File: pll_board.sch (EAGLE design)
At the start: 86 parts, among them U1 SI5351C, U3 MCP47X6, U4 LD117AS33TR, U5 74AC74D, X0 SMA-142-0711-871/876, X1 SMA-142-0711-871/876, X2 SMA-142-0711-871/876, X3 SMA-142-0711-871/876, X4 SMA-142-0711-871/876, X5 SMA-142-0711-871/876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

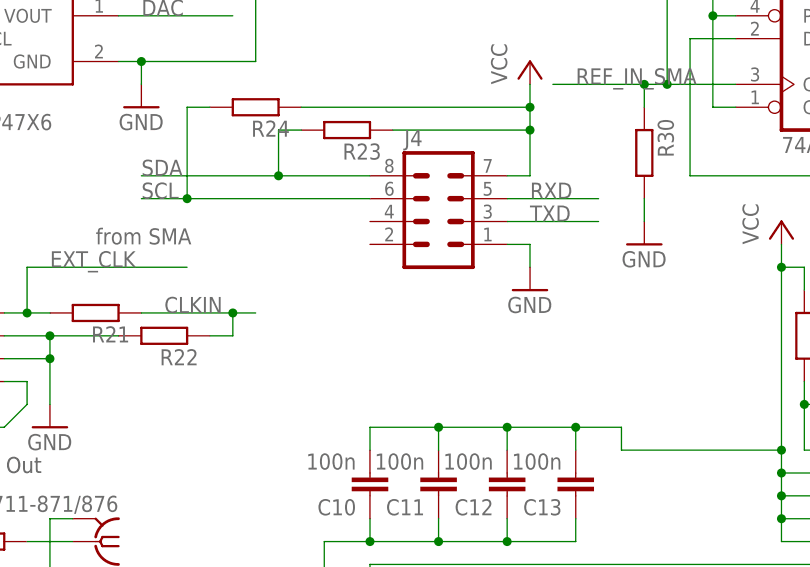
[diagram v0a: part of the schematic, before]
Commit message: Add USB +5V on i2c/uart connector.
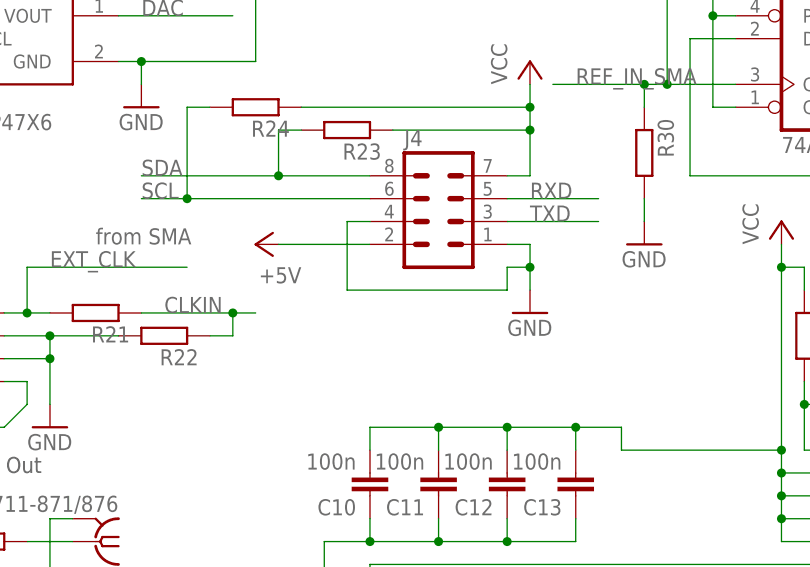
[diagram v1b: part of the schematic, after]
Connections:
- net +5V: now also J4.2
- net GND: now also J4.4
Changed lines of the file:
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@@
 <part name="GND16" library="supply1" deviceset="GND" device=""/>
 <part name="C15" library="rcl" deviceset="C-EU" device="C0805" value="100n"/>
+<part name="P+13" library="supply1" deviceset="+5V" device=""/>
 </parts>
 <sheets>
@@
 <instance part="P+9" gate="VCC" x="66.04" y="124.46"/>
 <instance part="J4" gate="G$1" x="137.16" y="137.16"/>
-<instance part="GND12" gate="1" x="147.32" y="127"/>
+<instance part="GND12" gate="1" x="147.32" y="124.46"/>
 <instance part="P+10" gate="VCC" x="147.32" y="152.4"/>
 <instance part="R23" gate="G$1" x="127" y="144.78" rot="R180"/>
@@
 <instance part="GND16" gate="1" x="236.22" y="132.08"/>
 <instance part="C15" gate="G$1" x="246.38" y="144.78" rot="R270"/>
+<instance part="P+13" gate="1" x="116.84" y="132.08" rot="R90"/>
 </instances>
 <busses>
@@
 <pinref part="GND12" gate="1" pin="GND"/>
 <wire x1="147.32" y1="132.08" x2="147.32" y2="129.54" width="0.1524" layer="91"/>
+<pinref part="J4" gate="G$1" pin="4"/>
+<wire x1="147.32" y1="129.54" x2="147.32" y2="127" width="0.1524" layer="91"/>
+<wire x1="129.54" y1="134.62" x2="127" y2="134.62" width="0.1524" layer="91"/>
+<wire x1="127" y1="134.62" x2="127" y2="127" width="0.1524" layer="91"/>
+<wire x1="127" y1="127" x2="144.78" y2="127" width="0.1524" layer="91"/>
+<wire x1="144.78" y1="127" x2="144.78" y2="129.54" width="0.1524" layer="91"/>
+<wire x1="144.78" y1="129.54" x2="147.32" y2="129.54" width="0.1524" layer="91"/>
+<junction x="147.32" y="129.54"/>
 </segment>
 <segment>
@@
 <junction x="177.8" y="86.36"/>
 </segment>
-</net>
+<segment>
+<pinref part="J4" gate="G$1" pin="2"/>
+<wire x1="129.54" y1="132.08" x2="119.38" y2="132.08" width="0.1524" layer="91"/>
+<pinref part="P+13" gate="1" pin="+5V"/>
+</segment>
+</net>
